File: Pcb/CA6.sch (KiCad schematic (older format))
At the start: 129 parts, among them J1 MICRO_USB, J2 BAT_CON, J3 MODULE_0, J4 MODULE_2, J5 MODULE_1, J6 AUX, J8 MODULE_3, P1 JTAG, P2 Connection Card, Q1 BSS138P, Q10 BSS138P, Q11 BSS138P, Q12 BSS138P, Q13 BSS138P, Q14 BSS138P, Q15 BSS138P, Q16 BSS138P, Q2 BSS138P, Q3 BSS138P, Q4 BSS138P, Q5 BSS138P, Q6 BSS138P, Q7 BSS138P, Q8 BSS138P, Q9 BSS138P, SW1 ERASE, SW2 USB/BATTERY, SW3 RESET, U1 L_PIPE, U12 VREG_33, U14 EEPROM, U15 L_PIPE, U16 ATSAM3X8EA-AU_LQFP-144, U2 L_PIPE, U3 L_PIPE, U4 L_PIPE, U5 L_PIPE, U6 L_PIPE, U7 L_PIPE, U8 L_PIPE, X1 HOLE, X2 HOLE, X3 HOLE, X4 HOLE, X7 CRYSTAL_4, X8 32khz

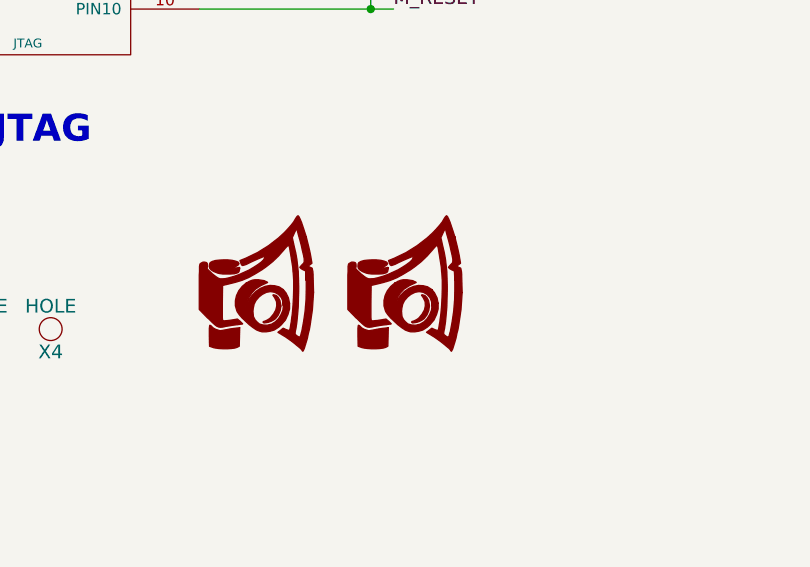
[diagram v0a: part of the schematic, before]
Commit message: Update gerbers and remove logo off back of pcb
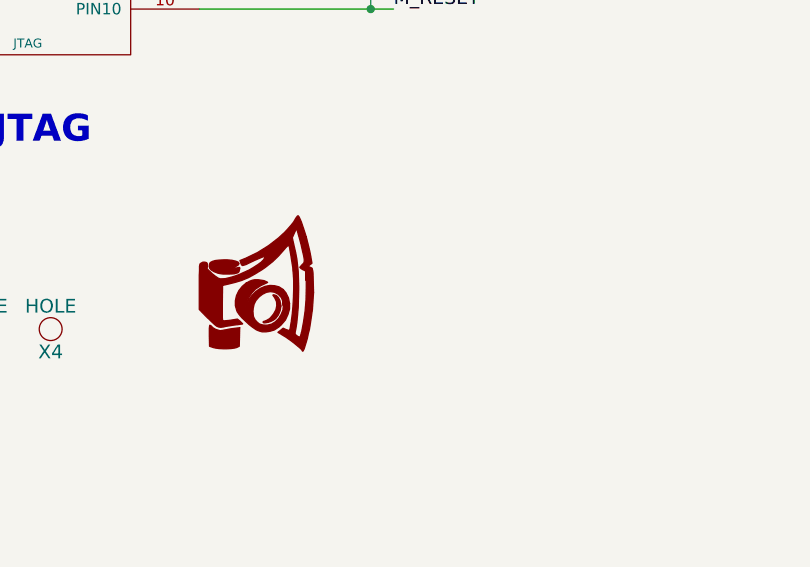
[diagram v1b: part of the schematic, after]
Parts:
- removed LOGO2: CA_LOGO_150, CA6:CA_Logo_15mm, symbol CA_Logo_150
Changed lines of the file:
@@
 LIBS:CA6
 LIBS:device
-LIBS:CA6-cache
 EELAYER 25 0
 EELAYER END
@@
 	1    0    0    -1
 $EndComp
-$Comp
-L CA_Logo_150 LOGO2
-U 1 1 544AEA8D
-P 3700 3950
-F 0 "LOGO2" H 3700 3677 60  0001 C CNN
-F 1 "CA_LOGO_150" H 3700 4223 60  0001 C CNN
-F 2 "CA6:CA_Logo_15mm" H 3700 3950 60  0001 C CNN
-F 3 "" H 3700 3950 60  0000 C CNN
-	1    3700 3950
-	1    0    0    -1
-$EndComp

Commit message: Update card header to have 2 more pins -- now a 6x2 header
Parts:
- removed P2: Connection Card, Socket_Strips:Socket_Strip_Straight_1x10_Pitch2.54mm, symbol JTAG_20021121-00010C4LF
- added P2: Connection_Card, Socket_Strips:Socket_Strip_Straight_2x06_Pitch2.54mm, symbol CONN_02X06
- added X5: HOLE, CA6:HOLE_3.0mm, symbol HOLE
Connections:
- net 3V3: now also P2.2 (P2)
- net AUX02: now also U16.142 (PB23); no longer U16.141 (PB22)
- net AUX03: now also U16.141 (PB22); no longer U16.140 (PB14)
- net AUX04: now also U16.140 (PB14); no longer U16.138 (PC27)
- net AUX05: now also U16.139 (PC28); no longer U16.137 (PC26)
- net AUX06: now also U16.138 (PC27); no longer U16.136 (PC25)
- net AUX07: now also U16.137 (PC26); no longer U16.135 (PC24)
- net AUX08: now also U16.136 (PC25); no longer U16.134 (PC23)
- net AUX09: now also U16.135 (PC24); no longer U16.133 (PC22)
- net AUX10: now also U16.134 (PC23); no longer U16.132 (PC21)
- net AUX11: now also U16.133 (PC22); no longer U16.131 (PC20)
- net AUX12: now also U16.132 (PC21); no longer U16.128 (PB10)
- net AUX13: now also U16.131 (PC20); no longer U16.127 (PB9)
- net AUX14: now also U16.128 (PB10); no longer U16.123 (PB8)
- net AUX15: now also U16.127 (PB9); no longer U16.122 (PB7)
- net AUX16: now also U16.123 (PB8); no longer U16.121 (PB6)
- net AUX17: now also U16.122 (PB7); no longer U16.120 (PB5)
- net AUX18: now also U16.121 (PB6); no longer U16.119 (PB4)
- net AUX19: now also U16.120 (PB5); no longer U16.118 (PB3)
- net AUX20: now also U16.119 (PB4); no longer U16.117 (PC10)
- net AUX21: now also U16.118 (PB3); no longer U16.116 (PC4)
- net AUX22: now also U16.117 (PC10); no longer U16.115 (PB2)
- net AUX23: now also U16.116 (PC4); no longer U16.114 (PB1)
- net AUX24: now also U16.115 (PB2); no longer U16.113 (PB0)
- net AUX25: now also U16.114 (PB1); no longer U16.112 (PA29)
- net AUX26: now also U16.113 (PB0); no longer U16.103 (PC30)
- net AUX27: now also U16.112 (PA29); no longer U16.102 (PC29)
- net AUX28: now also U16.103 (PC30); no longer U16.101 (PC19)
- net AUX29: now also U16.102 (PC29); no longer U16.100 (PC18)
- net AUX30: now also U16.101 (PC19); no longer U16.99 (PC17)
- net AUX31: now also U16.100 (PC18); no longer U16.98 (PC16)
- net AUX32: now also U16.99 (PC17); no longer U16.97 (PC15)
- net AUX33: now also U16.98 (PC16); no longer U16.96 (PC14)
- net AUX34: now also U16.97 (PC15); no longer U16.95 (PC13)
- net AUX35: now also U16.96 (PC14); no longer U16.94 (PC12)
- net AUX36: now also U16.95 (PC13); no longer U16.93 (PC11)
- net AUX37: now also U16.94 (PC12); no longer U16.92 (PB21)
- net AUX38: now also U16.93 (PC11); no longer U16.91 (PB20)
- net AUX39: now also U16.92 (PB21); no longer U16.90 (PB19)
- net AUX40: now also U16.91 (PB20); no longer U16.89 (PB18)
- net AUX41: now also U16.90 (PB19); no longer U16.77 (PB16)
- net AUX42: now also U16.89 (PB18); no longer U16.76 (PB15)
- net AUX43: now also U16.77 (PB16); no longer U16.72 (PA20)
- net AUX44: now also U16.76 (PB15); no longer U16.71 (PA19)
- net AUX45: now also U16.72 (PA20); no longer U16.68 (PB27)
- net AUX46: now also U16.71 (PA19); no longer U16.67 (PC9)
- net AUX47: now also U16.68 (PB27); no longer U16.66 (PC8)
- net CAM0F: now also U16.143 (PB24); no longer U16.142 (PB23)
- net CAM0S: now also U16.144 (PB25); no longer U16.143 (PB24)
- net CAM1F: now also U16.1 (PB26); no longer U16.144 (PB25)
- net CAM1S: now also U16.13 (PD0); no longer U16.1 (PB26)
- net CAM2F: now also U16.14 (PD1); no longer U16.13 (PD0)
- net CAM2S: now also U16.15 (PD2); no longer U16.14 (PD1)
- net CAM3F: now also U16.16 (PD3); no longer U16.15 (PD2)
- net CAM3S: now also U16.19 (PD6); no longer U16.16 (PD3)
- net CAM4F: now also U16.20 (PD7); no longer U16.19 (PD6)
- net CAM4S: now also U16.21 (PD8); no longer U16.20 (PD7)
- net CAM5F: now also U16.22 (PD9); no longer U16.21 (PD8)
- net CAM5S: now also U16.23 (PA0); no longer U16.22 (PD9)
- net CAM6F: now also U16.24 (PA1); no longer U16.23 (PA0)
- net CAM6S: now also U16.25 (PA5); no longer U16.24 (PA1)
- net CAM7F: now also U16.26 (PA7); no longer U16.25 (PA5)
- net CAM7S: now also U16.32 (PD10); no longer U16.26 (PA7)
- net CC_CTS: now also P2.7 (P7)
- net CC_G_LED: now also P2.4 (P4)
- net CC_PROG: now also U16.63 (PC5), P2.5 (P5); no longer U16.59 (PC2)
- net CC_RESET: now also U16.60 (PC3), P2.6 (P6); no longer U16.55 (PC1)
- net CC_RTS: now also P2.8 (P8)
- net CC_RX: now also P2.10 (P10)
- net CC_R_LED: now also P2.3 (P3)
- net CC_TX: now also P2.9 (P9)
- net GND: now also P2.1 (P1)
- net MOD0_ID: now also U16.67 (PC9); no longer U16.65 (PC7)
- net MOD1_ID: now also U16.66 (PC8); no longer U16.64 (PC6)
- net MOD2_ID: now also U16.65 (PC7); no longer U16.63 (PC5)
- net MOD3_ID: now also U16.64 (PC6); no longer U16.60 (PC3)
- new net CC_EXT0: P2.11 (P11), U16.59 (PC2)
- new net CC_EXT1: P2.12 (P12), U16.55 (PC1)
- no-connect marks 7 -> 5
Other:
- moved on the sheet: C23, C34, D1, R22, R30, U15

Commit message: Add new footprints for rj45 and switch
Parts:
- J3, J4, J5, J8: footprint CA6:RJ45_RJHSE-5080 -> CA6:RJ45_pcbwing
- SW2: footprint CA6:EG_1224 -> CA6:Switch_pcbwing_right_3a_ts-13p
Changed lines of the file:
@@
 F 0 "SW2" H 7700 13900 39  0000 C CNN
 F 1 "USB/BATTERY" H 7650 13650 39  0000 C CNN
-F 2 "CA6:EG_1224" H 7700 13800 60  0001 C CNN
+F 2 "CA6:Switch_pcbwing_right_3a_ts-13p" H 7700 13800 60  0001 C CNN
 F 3 "" H 7700 13800 60  0000 C CNN
 	1    7700 13800
@@
 F 0 "J5" H 21725 7050 39  0000 C CNN
 F 1 "MODULE_1" H 21375 7050 39  0000 C CNN
-F 2 "CA6:RJ45_RJHSE-5080" H 21525 6550 60  0001 C CNN
+F 2 "CA6:RJ45_pcbwing" H 21525 6550 60  0001 C CNN
 F 3 "~" H 21525 6550 60  0000 C CNN
 	1    21550 6550
@@
 F 0 "J3" H 18975 7050 39  0000 C CNN
 F 1 "MODULE_0" H 18625 7050 39  0000 C CNN
-F 2 "CA6:RJ45_RJHSE-5080" H 18775 6550 60  0001 C CNN
+F 2 "CA6:RJ45_pcbwing" H 18775 6550 60  0001 C CNN
 F 3 "~" H 18775 6550 60  0000 C CNN
 	1    18800 6550
@@
 F 0 "J4" H 18975 8000 39  0000 C CNN
 F 1 "MODULE_2" H 18625 8000 39  0000 C CNN
-F 2 "CA6:RJ45_RJHSE-5080" H 18775 7500 60  0001 C CNN
+F 2 "CA6:RJ45_pcbwing" H 18775 7500 60  0001 C CNN
 F 3 "~" H 18775 7500 60  0000 C CNN
 	1    18800 7500
@@
 F 0 "J8" H 21725 8000 39  0000 C CNN
 F 1 "MODULE_3" H 21375 8000 39  0000 C CNN
-F 2 "CA6:RJ45_RJHSE-5080" H 21525 7500 60  0001 C CNN
+F 2 "CA6:RJ45_pcbwing" H 21525 7500 60  0001 C CNN
 F 3 "~" H 21525 7500 60  0000 C CNN
 	1    21550 7500

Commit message: Change camera port LEDs to 2 color LEDs Change to using vertical light pipes that stick into case instead of 90 degree light pipes that stick to PCB Completely reworked how camera triggering works to use buffer chip.  Many more chips, but it should be more reliable Removed eeprom and changed that pin to a button that can put the esp8266 into programming mode (instead of using dev module button I had previously proposed) Change Reset/Erase buttons to SMD buttons Changed Camera/aux pins (through aux 25) so all the cam ports use port B to make faster triggering of camera ports Integrate esp8266 card onto main pcb.  Left the 12 pins for connection cards and put in jumpers that are connected by default, but could be cut. Change pin labeling on the module ports
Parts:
- removed C10, C23: 0.1uf, CA6:c_0603, symbol C
- removed C34: 10uf, CA6:c_1206, symbol C
- removed D10, D2, D4, D5, D6, D7, D8, D9: LED, LEDs:LED_0805, symbol LED
- removed U1, U15, U2, U3, U4, U5, U6, U7, U8: L_PIPE, CA6:SLP3-150-100-R, symbol LED_LIGHT_PIPE
- removed U14: EEPROM, CA6:SOT-23_11AA160, symbol 11AA160
- added C16, C18: 10uf, CA6:c_1206, symbol C
- added C23, C26: 100uf, CA6:c_elec_6.3x5.7, symbol CAP_ELEC
- added C27: 10uF, CA6:c_1206, symbol CAP_ELEC
- added D2, D3, D4, D5, D6, D7, D8, D9: LED2C, CA6:LED-SOT-23, symbol LED2C
- added JP10, JP2, JP3, JP4, JP5, JP6, JP7, JP8, JP9: Jumper_NC_Small, CA6:Jumper_connected, symbol Jumper_NC_Small
- added P3: ESP-Programming-FTDI, Socket_Strips:Socket_Strip_Straight_1x06_Pitch2.54mm, symbol FTDI
- added R1, R10, R11, R12, R13, R14, R15, R16, R61, R63, R64, R9: 10K, CA6:SM0603_Resistor, symbol R
- added R24, R33, R34, R37, R38, R41, R42, R45, R46, R49, R50, R53, R54, R57, R58: 274R, CA6:SM0603_Resistor, symbol R
- added R31, R32, R35, R36, R39, R40, R43, R44, R47, R48, R51, R52, R55, R56, R59, R60: 680R, CA6:SM0603_Resistor, symbol R
- added R62, R65: 4.7k, CA6:SM0603_Resistor, symbol R
- added SW4: BUTTON_0, CA6:PTS645_throughhole, symbol SW_TACTILE
- added U1, U2: 74LS244, Housings_SSOP:TSSOP-20_4.4x6.5mm_Pitch0.65mm, symbol 74LS244
- added U3: SN74AHC1G08, CA6:SOT-23-5_GATE, symbol SN74AHC1G08
- added U4: ESP-12E/F, CA6:ESP-12E-F-no-bottom-pads, symbol ESP-12E/F
- R2, R3, R4, R5, R6, R7, R8: value 680R -> 10K
- R22, R30: value 680R -> 274R
- R23: renamed from R1; value 680R -> 274R
- SW1, SW3: footprint CA6:PTS645_throughhole -> Buttons_Switches_SMD:SW_SPST_PTS645
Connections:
- net 3V3: now also C16.1, C18.1, JP6.1, U1.20 (VCC), U2.20 (VCC)
- net AUX02: now also U16.32 (PD10); no longer U16.142 (PB23)
- net AUX03: now also U16.26 (PA7); no longer U16.141 (PB22)
- net AUX04: now also U16.25 (PA5); no longer U16.140 (PB14)
- net AUX05: now also U16.24 (PA1); no longer U16.139 (PC28)
- net AUX06: now also U16.23 (PA0); no longer U16.138 (PC27)
- net AUX07: now also U16.22 (PD9); no longer U16.137 (PC26)
- net AUX08: now also U16.21 (PD8); no longer U16.136 (PC25)
- net AUX09: now also U16.20 (PD7); no longer U16.135 (PC24)
- net AUX10: now also U16.19 (PD6); no longer U16.134 (PC23)
- net AUX11: now also U16.16 (PD3); no longer U16.133 (PC22)
- net AUX12: now also U16.15 (PD2); no longer U16.132 (PC21)
- net AUX13: now also U16.14 (PD1); no longer U16.131 (PC20)
- net AUX14: now also U16.13 (PD0); no longer U16.128 (PB10)
- net AUX15: now also U16.139 (PC28); no longer U16.127 (PB9)
- net AUX16: now also U16.138 (PC27); no longer U16.123 (PB8)
- net AUX17: now also U16.137 (PC26); no longer U16.122 (PB7)
- net AUX18: now also U16.136 (PC25); no longer U16.121 (PB6)
- net AUX19: now also U16.135 (PC24); no longer U16.120 (PB5)
- net AUX20: now also U16.134 (PC23); no longer U16.119 (PB4)
- net AUX21: now also U16.133 (PC22); no longer U16.118 (PB3)
- net AUX22: now also U16.132 (PC21); no longer U16.117 (PC10)
- net AUX23: now also U16.131 (PC20); no longer U16.116 (PC4)
- net AUX24: now also U16.117 (PC10); no longer U16.115 (PB2)
- net AUX25: now also U16.116 (PC4); no longer U16.114 (PB1)
- net CAM0F: now also R5.1, U16.114 (PB1), U1.4 (I1a); no longer Q9.1 (G), U16.143 (PB24)
- net CAM0S: now also U16.115 (PB2), R1.1, U1.2 (I0a); no longer Q1.1 (G), R23.1, U16.144 (PB25)
- net CAM1F: now also U16.118 (PB3), R13.1, U1.8 (I3a); no longer Q10.1 (G), U16.1 (PB26)
- net CAM1S: now also U16.119 (PB4), R9.1, U1.6 (I2a); no longer Q2.1 (G), R2.1, U16.13 (PD0)
- net CAM2F: now also U16.120 (PB5), R10.1, U1.13 (I1b); no longer Q11.1 (G), U16.14 (PD1)
- net CAM2S: now also U16.121 (PB6), R14.1, U1.11 (I0b); no longer Q3.1 (G), R3.1, U16.15 (PD2)
- net CAM3F: now also R2.1, U16.122 (PB7), U1.17 (I3b); no longer Q12.1 (G), U16.16 (PD3)
- net CAM3S: now also R6.1, U16.123 (PB8), U1.15 (I2b); no longer Q4.1 (G), R4.1, U16.19 (PD6)
- net CAM4F: now also R7.1, U16.127 (PB9), U2.4 (I1a); no longer Q13.1 (G), U16.20 (PD7)
- net CAM4S: now also R3.1, U16.128 (PB10), U2.2 (I0a); no longer Q5.1 (G), R5.1, U16.21 (PD8)
- net CAM5F: now also U16.140 (PB14), R15.1, U2.8 (I3a); no longer Q14.1 (G), U16.22 (PD9)
- net CAM5S: now also U16.141 (PB22), R11.1, U2.6 (I2a); no longer Q6.1 (G), R6.1, U16.23 (PA0)
- net CAM6F: now also U16.142 (PB23), R12.1, U2.13 (I1b); no longer Q15.1 (G), U16.24 (PA1)
- net CAM6S: now also U16.143 (PB24), R16.1, U2.11 (I0b); no longer Q7.1 (G), R7.1, U16.25 (PA5)
- net CAM7F: now also R4.1, U16.144 (PB25), U2.17 (I3b); no longer Q16.1 (G), U16.26 (PA7)
- net CAM7S: now also U16.1 (PB26), U2.15 (I2b); no longer Q8.1 (G), U16.32 (PD10)
- net CC_CTS: now also JP3.2
- net CC_EXT0: now also JP5.2
- net CC_EXT1: now also JP10.1
- net CC_PROG: now also JP2.2
- net CC_RESET: now also JP7.1
- net CC_RTS: now also JP8.1
- net CC_RX: now also JP9.1
- net CC_TX: now also JP4.2
- net GND: now also R2.2, R3.2, R4.2, R5.2, R6.2, R7.2, R8.2, C16.2, C18.2, C23.2, C26.2, C27.2, D2.3, D3.3, D4.3, D5.3, D6.3, D7.3, D8.3, D9.3, P3.1 (GND), R1.2, R10.2, R11.2, R12.2, R13.2, R14.2, R15.2, R16.2, R63.1, R9.2, SW4.1, SW4.2, U1.1 (OEa), U1.10 (GND), U1.19 (OEb), U2.1 (OEa), U2.10 (GND), U2.19 (OEb), U3.3 (GND), U4.9 (GND)
- net VBUS: now also SW2.3; no longer SW2.1
- net at J2.2 (PM): now also SW2.1; no longer SW2.3
- net at R23.2: now also R31.2, U1.18 (O0a)
- net AUX_RX renamed AUX01_RX
- net AUX_TX renamed AUX00_TX
- net CC_G_LED renamed ESP_G_LED
- net ESP_G_LED: now also U4.13 (GPIO4)
- net CC_R_LED renamed ESP_R_LED
- net ESP_R_LED: now also U4.14 (GPIO5)
- net EEPROM_ID renamed BUTTON_0
- net BUTTON_0: now also SW4.3, SW4.4
- net MOD0_AN1 renamed MOD0p0_AN0
- net MOD0_ID renamed MOD0p3
- net MOD0_RX renamed MOD0p4_RX
- net MOD0_SCL renamed MOD0p1_SCL
- net MOD0_SDA renamed MOD0p2_SDA
- net MOD0_TX renamed MOD0p5_TX
- net MOD1_AN1 renamed MOD1p0_AN0
- net MOD1_ID renamed MOD1p3
- net MOD1_RX renamed MOD1p4_RX
- net MOD1_SCL renamed MOD1p1_SCL
- net MOD1_SDA renamed MOD1p2_SDA
- net MOD1_TX renamed MOD1p5_TX
- net MOD2_AN1 renamed MOD2p0_AN0
- net MOD2_AN2 renamed MOD2p1_AN1
- net MOD2_AN3 renamed MOD2p2_AN2
- net MOD2_AN4 renamed MOD2p4_AN3
- net MOD2_AN5 renamed MOD2p5_AN4
- net MOD2_ID renamed MOD2p3
- net MOD3_AN1 renamed MOD3p0_AN0
- net MOD3_CS renamed MOD3p5_CS
- net MOD3_ID renamed MOD3p3
- net MOD3_MISO renamed MOD3p2_MISO
- net MOD3_MOSI renamed MOD3p1_MOSI
- net MOD3_SCLK renamed MOD3p4_SCLK
- new net: Q9.1 (G), R32.1
- new net: Q1.1 (G), R31.1
- new net: Q10.1 (G), R36.1
- new net: Q2.1 (G), R35.1
- new net: Q11.1 (G), R40.1
- new net: Q3.1 (G), R39.1
- new net: Q12.1 (G), R44.1
- new net: Q4.1 (G), R43.1
- new net: Q13.1 (G), R48.1
- new net: Q5.1 (G), R47.1
- new net: Q14.1 (G), R52.1
- new net: Q6.1 (G), R51.1
- new net: Q15.1 (G), R56.1
- new net: Q7.1 (G), R55.1
- new net: Q16.1 (G), R60.1
- new net: Q8.1 (G), R59.1
- new net: D2.1, R23.1
- new net: D2.2, R24.1
- new net: R24.2, R32.2, U1.16 (O1a)
- new net: R34.2, R36.2, U1.12 (O3a)
- new net: R33.2, R35.2, U1.14 (O2a)
- new net: R42.2, R44.2, U1.3 (O3b)
- new net: R41.2, R43.2, U1.5 (O2b)
- new net: R38.2, R40.2, U1.7 (O1b)
- new net: R37.2, R39.2, U1.9 (O0b)
- new net: D3.1, R33.1
- new net: D3.2, R34.1
- new net: D4.1, R37.1
- new net: D4.2, R38.1
- new net: D5.1, R41.1
- new net: D5.2, R42.1
- new net: R64.1, U4.3 (CH_PD)
- new net: P3.4 (TXO), U3.2
- new net: R61.2, U4.11 (GPIO2)
- new net: U3.4, U4.15 (RXD)
- new net: D6.1, R45.1
- new net: R45.2, R47.2, U2.18 (O0a)
- new net: D6.2, R46.1
- new net: R46.2, R48.2, U2.16 (O1a)
- new net: R50.2, R52.2, U2.12 (O3a)
- new net: R49.2, R51.2, U2.14 (O2a)
- new net: R58.2, R60.2, U2.3 (O3b)
- new net: R57.2, R59.2, U2.5 (O2b)
- new net: R54.2, R56.2, U2.7 (O1b)
- new net: R53.2, R55.2, U2.9 (O0b)
- new net: D7.1, R49.1
- new net: D7.2, R50.1
- new net: D8.1, R53.1
- new net: D8.2, R54.1
- new net: D9.1, R57.1
- new net: D9.2, R58.1
- new net ESP_3V3: C23.1, C26.1, C27.1, JP6.2, R61.1, R62.1, R64.2, R65.2, U3.5 (VCC), U4.8 (VCC)
- new net ESP_CTS: JP3.1, R63.2, U4.10 (GPIO15)
- new net ESP_EXT0: JP5.1, U4.6 (GPIO12)
- new net ESP_EXT1: JP10.2, U4.5 (GPIO14)
- new net ESP_PROG: JP2.1, R62.2, U4.12 (GPIO0)
- new net ESP_RESET: JP7.2, R65.1, U4.1 (REST)
- new net ESP_RTS: JP8.2, U4.7 (GPIO13)
- new net ESP_RX: JP9.2, P3.5 (RXI), U4.16 (TXD)
- new net ESP_TX: JP4.1, U3.1
- no-connect marks 5 -> 16
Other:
- note removed: "EEPROM"
- moved on the sheet: BT1, C1, C11, C12, C13, C14, C15, C17, C19, C2, C20, C21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

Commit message: Add some 0.1uF caps
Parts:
- added C10, C34, C35: 0.1uf, CA6:c_0603, symbol C
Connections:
- net 3V3: now also C34.1
- net 5V: now also C10.1
- net GND: now also C10.2, C34.2
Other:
- moved on the sheet: C5, C6, C7, C9

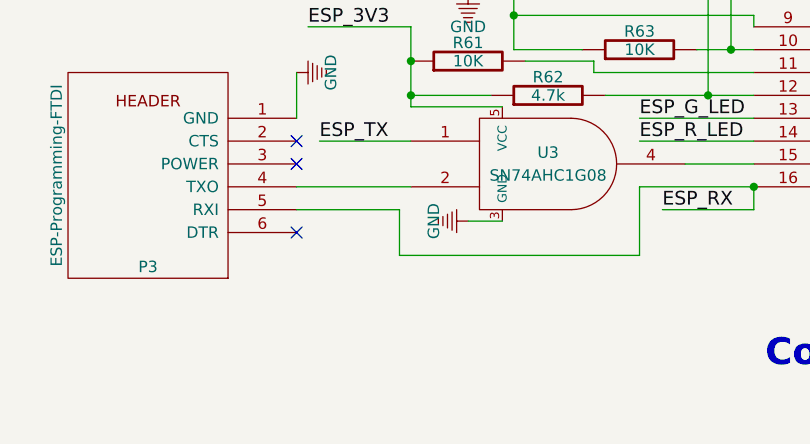
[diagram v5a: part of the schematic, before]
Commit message: Add a missing pullup resistor on the esp8266 programming circuit
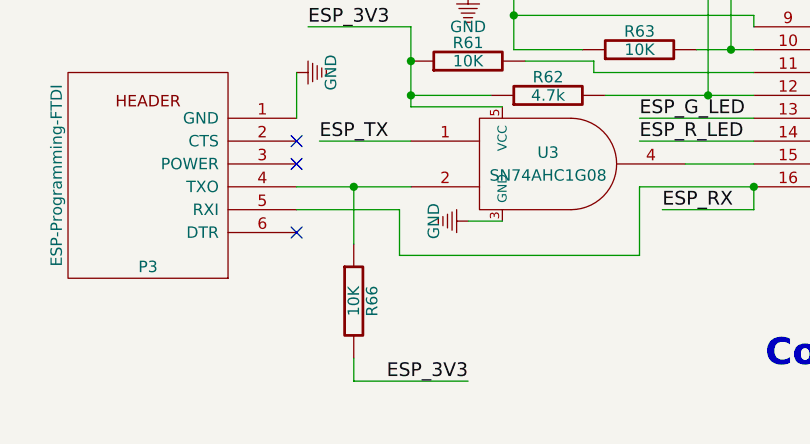
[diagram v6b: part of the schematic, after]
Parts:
- added R66: 10K, CA6:SM0603_Resistor, symbol R
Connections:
- net ESP_3V3: now also R66.2
- net at P3.4 (TXO), U3.2: now also R66.1
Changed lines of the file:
@@
 	1    0    0    -1
 $EndComp
+$Comp
+L R R66
+U 1 1 5A02D7A7
+P 17750 14300
+F 0 "R66" V 17830 14300 50  0000 C CNN
+F 1 "10K" V 17750 14300 50  0000 C CNN
+F 2 "CA6:SM0603_Resistor" V 17680 14300 50  0001 C CNN
+F 3 "" H 17750 14300 50  0000 C CNN
+	1    17750 14300
+	1    0    0    -1
+$EndComp
+Wire Wire Line
+	17750 13800 17750 14050
+Connection ~ 17750 13800
+Wire Wire Line
+	17750 14550 17750 14650
+Wire Wire Line
+	17750 14650 18250 14650
+Text Label 18250 14650 2    60   ~ 0
+ESP_3V3
 $EndSCHEMATC

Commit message: Do an initial placement of the parts on the CA6 PCB
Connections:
- net ESP_3V3: now also C35.2
- net GND: now also C35.1
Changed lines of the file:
@@
 Text Label 18250 14650 2    60   ~ 0
 ESP_3V3
+Connection ~ 22200 13100
+Connection ~ 22200 12700
 $EndSCHEMATC
